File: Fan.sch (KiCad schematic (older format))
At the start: 9 parts

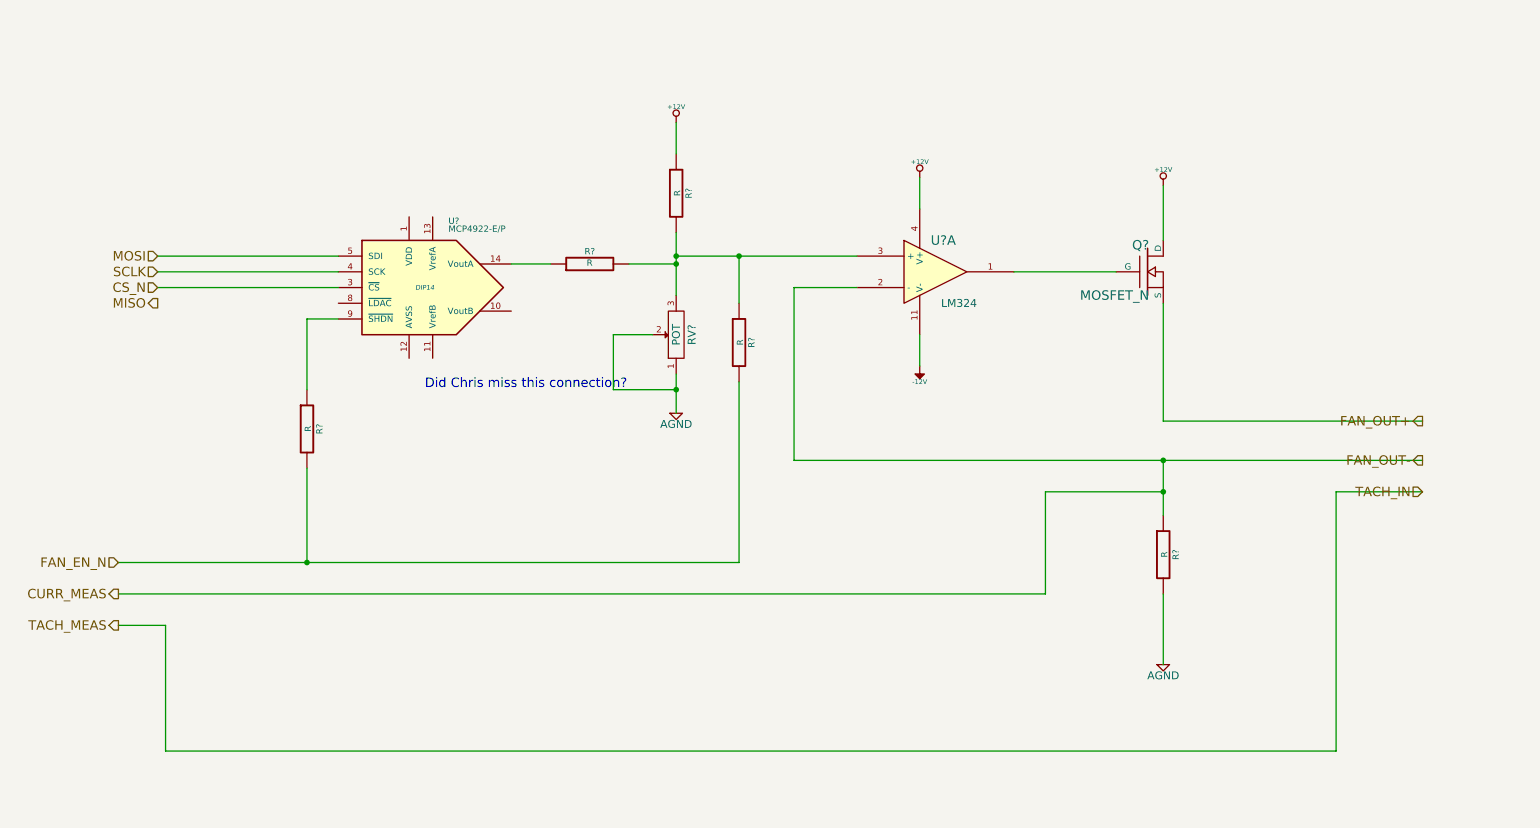
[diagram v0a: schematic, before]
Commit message: Fan/Current Module Rework
Rework of the Fan/Current module
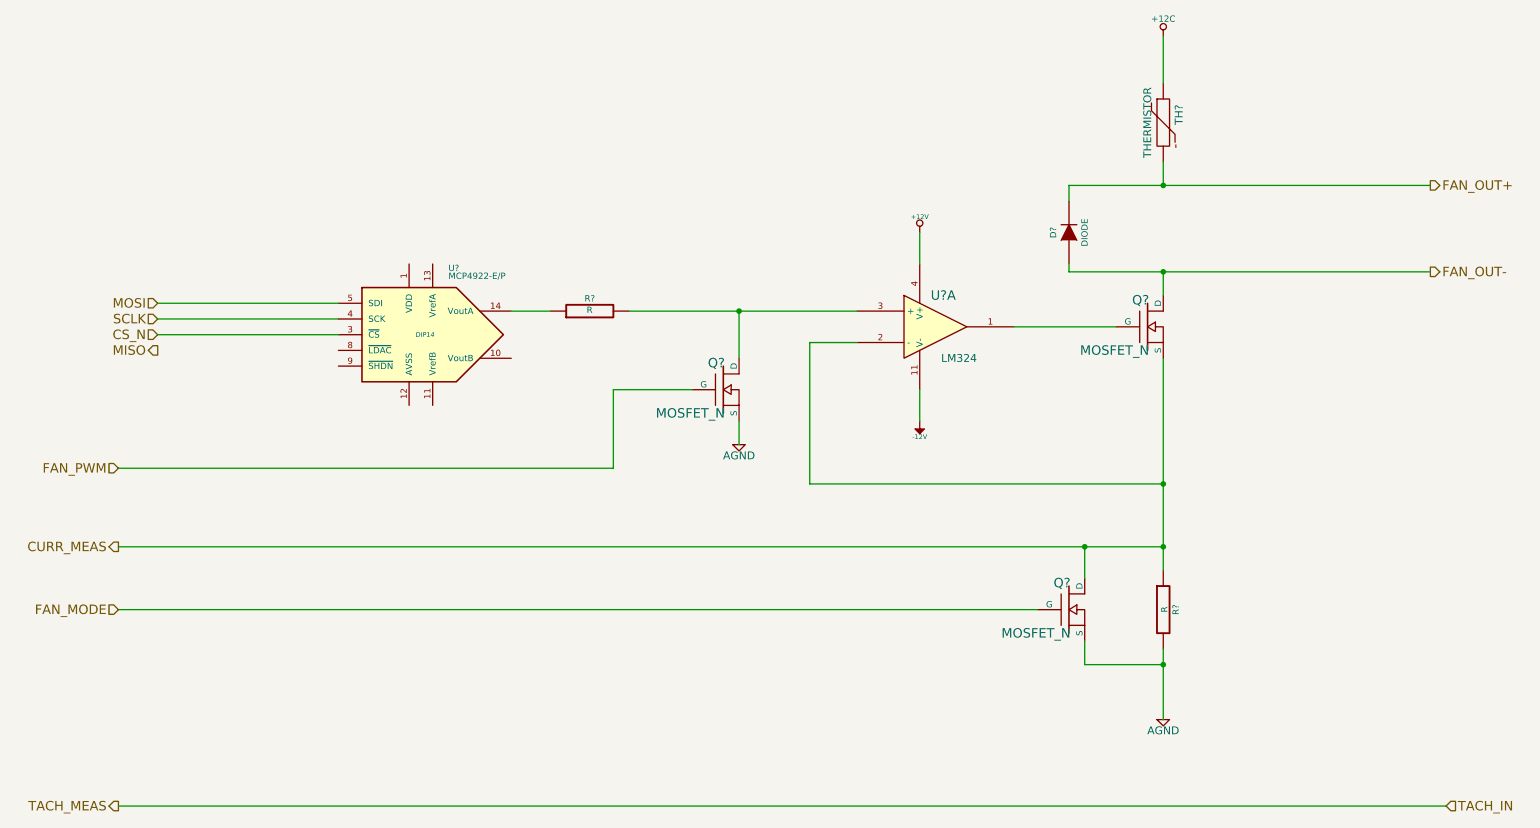
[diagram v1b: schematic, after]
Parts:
- removed R? (x3): R, ~, symbol R
- removed RV?: POT, ~, symbol POT
- added D?: DIODE, ~, symbol DIODE
- added Q? (x2): MOSFET_N, ~, symbol MOSFET_N
- added TH?: THERMISTOR, ~, symbol THERMISTOR
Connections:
- net +12V: no longer Q?.D
- net AGND: now also Q?.S, Q?.S
- net CURR_MEAS: now also Q?.S, Q?.D
- net FAN_OUT+: now also D?.2 (K), TH?.2; no longer Q?.S
- net at R?.2, U?.3 (+): now also Q?.D
- new net +12C: TH?.1
- new net FAN_MODE: Q?.G
- new net FAN_OUT-: D?.1 (A), Q?.D
- new net FAN_PWM: Q?.G
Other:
- note removed: "Did Chris miss this connection?"
- moved on the sheet: Q?, R?, U?, U?A
